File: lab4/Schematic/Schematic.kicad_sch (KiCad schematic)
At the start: 404 parts, among them IC1 TPS564252DRLR, IC2 TPS564252DRLR, IC3 TPS564252DRLR, IC4 TPS564252DRLR, IC5 TPS564252DRLR, IC6 TPS564252DRLR, J1 XT60-M, J10 CANA_Z1, J11 CANA_Z1, J12 CANA_Z1, J13 CANA_Z1, J14 CANA_Z1, J15 CANA_Z1, J16 Conn_01x03_Pin, J17 Conn_01x03_Pin, J2 Z2_SWD, J3 Z2_SWD, J4 Z3_USART, J5 Raspberry_Pi_4, J6 Z3_USART, J7 MOTOR_RIGHT, J8 MOTOR_LEFT, J9 SERVO, Q2 IRF4905, U1 MCP2515-xST, U10 SN65HVD230, U11 MCP2515-xST, U12 SN65HVD230, U13 MCP2515-xST, U14 SN65HVD230, U15 MCP2515-xST, U16 SN65HVD230, U17 MCP2515-xST, U18 SN65HVD230, U2 ACS712xLCTR-05B, U20 L298N, U3 STM32F401RETx, U4 ACS712xLCTR-05B, U5 INA181, U7 STM32F401RETx, U8 SN65HVD230, U9 MCP2515-xST, Y1 CX3225SB16000H0FLJCC, Y2 CX3225SB16000H0FLJCC, Y3 CX3225SB16000H0FLJCC, Y4 CX3225SB16000H0FLJCC, Y5 CX3225SB16000H0FLJCC, Y6 CX3225SB16000H0FLJCC, Y7 ABS25-32.768KHZ-6-T, Y8 ABS25-32.768KHZ-6-T

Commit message: Power input and protections done with pours.
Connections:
- net +12V: now also J16.3 (Pin_3), J17.3 (Pin_3); no longer J16.1 (Pin_1), J17.1 (Pin_1)
- net GND: now also J1.1 (NEG), J16.1 (Pin_1), J17.1 (Pin_1); no longer J1.N (NEG), J16.3 (Pin_3), J17.3 (Pin_3)
- net at F2.1_1, F2.1_2: now also J1.2 (POS); no longer J1.P (POS)
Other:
- moved on the sheet: J16, J17
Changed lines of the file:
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@@
 	(wire
 		(pts
+			(xy 53.34 91.44) (xy 60.96 91.44)
+		)
+		(stroke
+			(width 0)
+			(type default)
+		)
+	)
+	(wire
+		(pts
 			(xy 664.21 345.44) (xy 664.21 342.9)
 		)
@@
 	(wire
 		(pts
+			(xy 53.34 104.14) (xy 60.96 104.14)
+		)
+		(stroke
+			(width 0)
+			(type default)
+		)
+	)
+	(wire
+		(pts
 			(xy 505.46 448.31) (xy 505.46 450.85)
 		)
@@
 	(wire
 		(pts
+			(xy 43.18 86.36) (xy 60.96 86.36)
+		)
+		(stroke
+			(width 0)
+			(type default)
+		)
+	)
+	(wire
+		(pts
 			(xy 486.41 285.75) (xy 497.84 285.75)
 		)
@@
 	(wire
 		(pts
+			(xy 43.18 99.06) (xy 60.96 99.06)
+		)
+		(stroke
+			(width 0)
+			(type default)
+		)
+	)
+	(wire
+		(pts
 			(xy 123.19 396.24) (xy 123.19 417.83)
 		)
@@
 	(wire
 		(pts
-			(xy 60.96 99.06) (xy 43.18 99.06)
-		)
-		(stroke
-			(width 0)
-			(type default)
-		)
-	)
-	(wire
-		(pts
 			(xy 245.11 45.72) (xy 247.65 45.72)
 		)
@@
 	(wire
 		(pts
-			(xy 17.78 101.6) (xy 60.96 101.6)
-		)
-		(stroke
-			(width 0)
-			(type default)
-		)
-	)
-	(wire
-		(pts
 			(xy 458.47 280.67) (xy 466.09 280.67)
 		)
@@
 	(wire
 		(pts
-			(xy 53.34 91.44) (xy 60.96 91.44)
-		)
-		(stroke
-			(width 0)
-			(type default)
-		)
-	)
-	(wire
-		(pts
 			(xy 275.59 173.99) (xy 275.59 176.53)
 		)
@@
 	(wire
 		(pts
-			(xy 20.32 88.9) (xy 60.96 88.9)
-		)
-		(stroke
-			(width 0)
-			(type default)
-		)
-	)
-	(wire
-		(pts
 			(xy 365.76 207.01) (xy 365.76 219.71)
 		)
@@
 	(wire
 		(pts
-			(xy 60.96 86.36) (xy 43.18 86.36)
-		)
-		(stroke
-			(width 0)
-			(type default)
-		)
-	)
-	(wire
-		(pts
 			(xy 560.07 91.44) (xy 581.66 91.44)
 		)
@@
 	(wire
 		(pts
+			(xy 17.78 101.6) (xy 60.96 101.6)
+		)
+		(stroke
+			(width 0)
+			(type default)
+		)
+	)
+	(wire
+		(pts
 			(xy 436.88 419.1) (xy 485.14 419.1)
 		)
@@
 	(wire
 		(pts
-			(xy 53.34 104.14) (xy 60.96 104.14)
-		)
-		(stroke
-			(width 0)
-			(type default)
-		)
-	)
-	(wire
-		(pts
 			(xy 736.6 58.42) (xy 736.6 55.88)
 		)
@@
 	(wire
 		(pts
+			(xy 20.32 88.9) (xy 60.96 88.9)
+		)
+		(stroke
+			(width 0)
+			(type default)
+		)
+	)
+	(wire
+		(pts
 			(xy 60.96 444.5) (xy 97.79 444.5)
 		)
@@
 	(symbol
 		(lib_id "Connector:Conn_01x03_Pin")
-		(at 66.04 101.6 0)
-		(mirror y)
+		(at 66.04 101.6 180)
 		(unit 1)
 		(body_style 1)
@@
 		(dnp no)
 		(property "Reference" "J16"
-			(at 65.405 93.98 0)
+			(at 65.405 109.22 0)
 			(show_name no)
 			(do_not_autoplace no)
@@
 		)
 		(property "Value" "Conn_01x03_Pin"
-			(at 65.405 96.52 0)
+			(at 65.405 106.68 0)
 			(show_name no)
 			(do_not_autoplace no)
@@
 			)
 		)
-		(pin "N"
+		(pin "2"
 		)
-		(pin "P"
+		(pin "1"
 		)
 		(instances
@@
 	(symbol
 		(lib_id "Connector:Conn_01x03_Pin")
-		(at 66.04 88.9 0)
-		(mirror y)
+		(at 66.04 88.9 180)
 		(unit 1)
 		(body_style 1)
@@
 		(dnp no)
 		(property "Reference" "J17"
-			(at 65.405 81.28 0)
+			(at 65.405 96.52 0)
 			(show_name no)
 			(do_not_autoplace no)
@@
 		)
 		(property "Value" "Conn_01x03_Pin"
-			(at 65.405 83.82 0)
+			(at 65.405 93.98 0)
 			(show_name no)
 			(do_not_autoplace no)

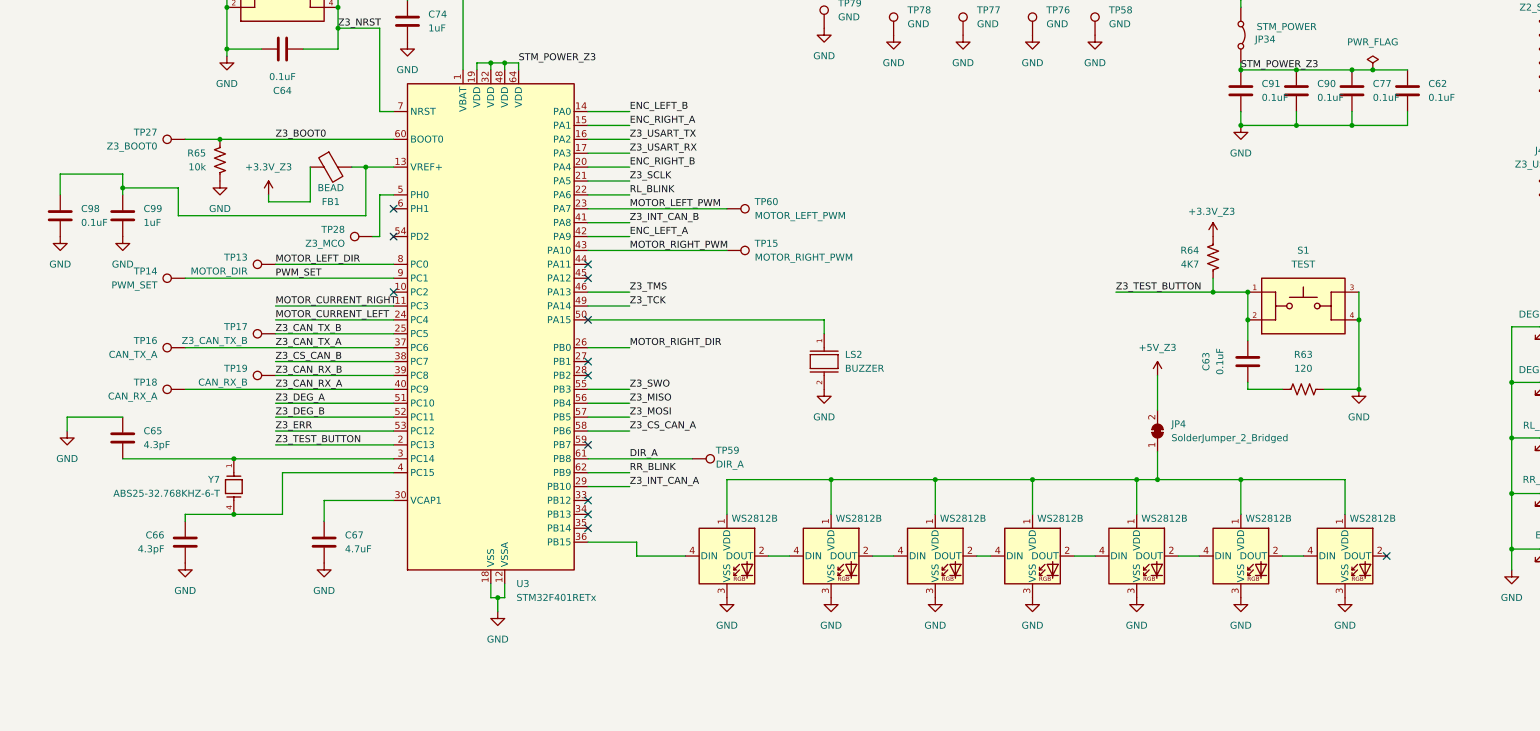
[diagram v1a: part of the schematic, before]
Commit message: Initial pin assignment change.
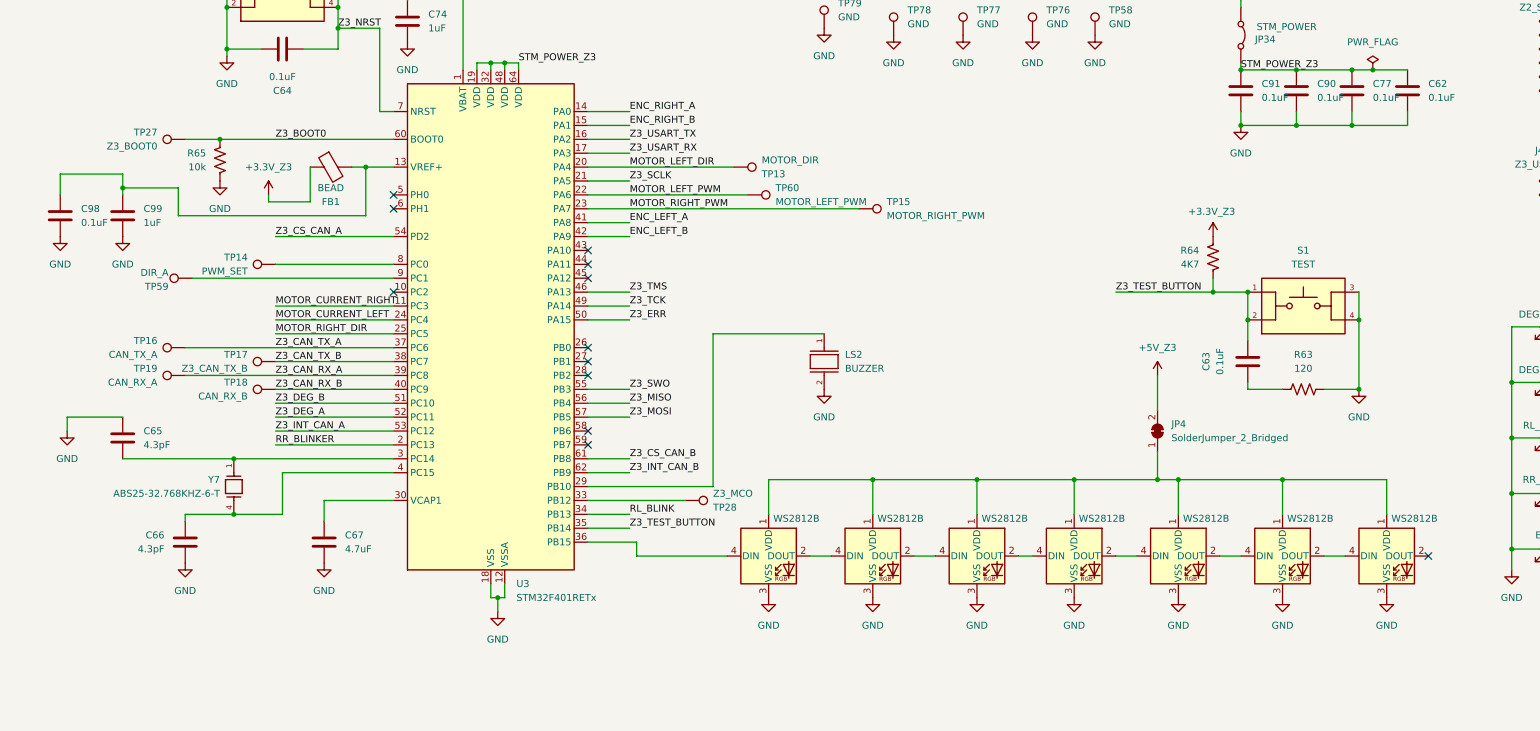
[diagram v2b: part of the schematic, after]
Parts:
- TP18: value CAN_RX_A -> CAN_RX_B
- TP19: value CAN_RX_B -> CAN_RX_A
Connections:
- net ENC_LEFT_A: now also U3.41 (PA8); no longer U3.42 (PA9)
- net ENC_LEFT_B: now also U3.42 (PA9); no longer U3.14 (PA0)
- net ENC_RIGHT_A: now also U3.14 (PA0); no longer U3.15 (PA1)
- net ENC_RIGHT_B: now also U3.15 (PA1); no longer U3.20 (PA4)
- net MOTOR_LEFT_DIR: now also U3.20 (PA4); no longer U3.8 (PC0)
- net MOTOR_LEFT_PWM: now also U3.22 (PA6); no longer U3.23 (PA7)
- net MOTOR_RIGHT_DIR: now also U3.25 (PC5); no longer U3.26 (PB0)
- net MOTOR_RIGHT_PWM: now also U3.23 (PA7); no longer U3.43 (PA10)
- net RL_BLINK: now also U3.34 (PB13); no longer U3.22 (PA6)
- net RR_BLINK: no longer U3.62 (PB9)
- net Z3_CAN_RX_A: now also TP19.1, U3.39 (PC8); no longer TP18.1, U3.40 (PC9)
- net Z3_CAN_RX_B: now also TP18.1, U3.40 (PC9); no longer TP19.1, U3.39 (PC8)
- net Z3_CAN_TX_B: now also U3.38 (PC7); no longer U3.25 (PC5)
- net Z3_CS_CAN_A: now also U3.54 (PD2); no longer U3.58 (PB6)
- net Z3_CS_CAN_B: now also U3.61 (PB8); no longer U3.38 (PC7)
- net Z3_DEG_A: now also U3.52 (PC11); no longer U3.51 (PC10)
- net Z3_DEG_B: now also U3.51 (PC10); no longer U3.52 (PC11)
- net Z3_ERR: now also U3.50 (PA15); no longer U3.53 (PC12)
- net Z3_INT_CAN_A: now also U3.53 (PC12); no longer U3.29 (PB10)
- net Z3_INT_CAN_B: now also U3.62 (PB9); no longer U3.41 (PA8)
- net Z3_TEST_BUTTON: now also U3.35 (PB14); no longer U3.2 (PC13)
- net at TP28.1: now also U3.33 (PB12); no longer U3.5 (PH0)
- net at LS2.1: now also U3.29 (PB10); no longer U3.50 (PA15)
- net DIR_A: no longer names the net of TP59.1
- net DIR_A: now also U3.9 (PC1); no longer U3.61 (PB8)
- net PWM_SET: no longer names the net of TP14.1
- net PWM_SET: now also U3.8 (PC0); no longer U3.9 (PC1)
- new net RR_BLINKER: U3.2 (PC13)
- no-connect marks 89 -> 88
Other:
- moved on the sheet: TP13, TP14, TP15, TP17, TP18, TP19, TP28, TP59, TP60

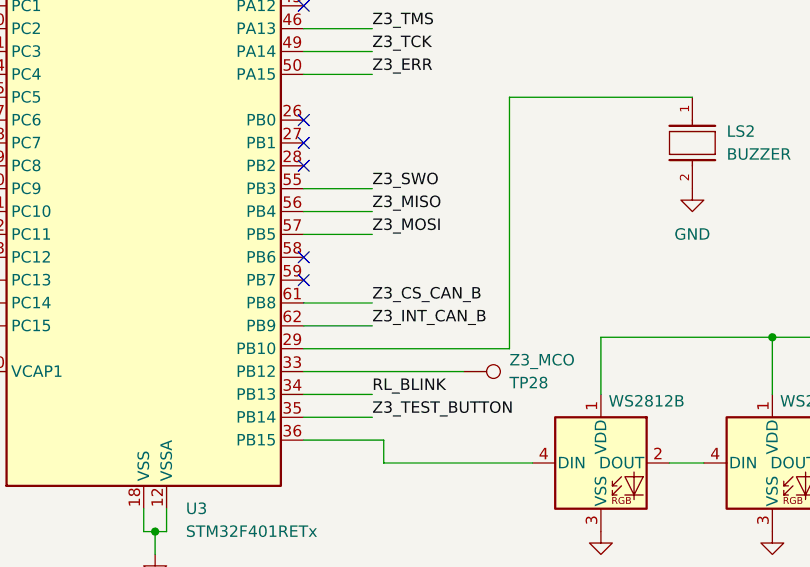
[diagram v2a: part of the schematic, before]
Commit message: Fixed ENC and CAN_INT exti cofnflict.
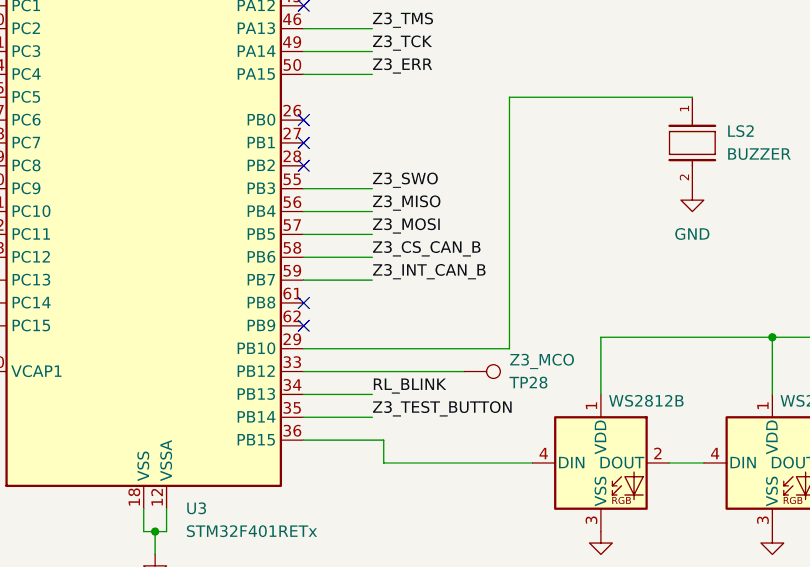
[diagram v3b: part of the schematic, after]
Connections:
- net Z3_CS_CAN_B: now also U3.58 (PB6); no longer U3.61 (PB8)
- net Z3_INT_CAN_B: now also U3.59 (PB7); no longer U3.62 (PB9)
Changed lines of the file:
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@@
 	)
 	(no_connect
-		(at 617.22 114.3)
-	)
-	(no_connect
 		(at 44.45 64.77)
 	)
@@
 	)
 	(no_connect
+		(at 617.22 119.38)
+	)
+	(no_connect
 		(at 267.97 222.25)
 	)
@@
 	)
 	(no_connect
-		(at 260.35 115.57)
+		(at 617.22 121.92)
 	)
 	(no_connect
-		(at 617.22 116.84)
+		(at 260.35 115.57)
 	)
 	(no_connect
@@
 	(wire
 		(pts
+			(xy 617.22 114.3) (xy 624.84 114.3)
+		)
+		(stroke
+			(width 0)
+			(type default)
+		)
+	)
+	(wire
+		(pts
 			(xy 713.74 88.9) (xy 731.52 88.9)
 		)
@@
 	(wire
 		(pts
-			(xy 624.84 121.92) (xy 617.22 121.92)
-		)
-		(stroke
-			(width 0)
-			(type default)
-		)
-	)
-	(wire
-		(pts
 			(xy 562.61 198.12) (xy 638.81 198.12)
 		)
@@
 	(wire
 		(pts
-			(xy 617.22 119.38) (xy 624.84 119.38)
-		)
-		(stroke
-			(width 0)
-			(type default)
-		)
-	)
-	(wire
-		(pts
 			(xy 110.49 64.77) (xy 114.3 64.77)
 		)
@@
 	(wire
 		(pts
+			(xy 617.22 116.84) (xy 624.84 116.84)
+		)
+		(stroke
+			(width 0)
+			(type default)
+		)
+	)
+	(wire
+		(pts
 			(xy 716.28 393.7) (xy 722.63 393.7)
 		)
@@
 	)
 	(label "Z3_CS_CAN_B"
-		(at 624.84 119.38 0)
+		(at 624.84 114.3 0)
 		(effects
 			(font
@@
 	)
 	(label "Z3_INT_CAN_B"
-		(at 624.84 121.92 0)
+		(at 624.84 116.84 0)
 		(effects
 			(font

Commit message: Logic level and v-reg for leds. Motor Driver heatsink. Fixed pth vs sm footprints. Misc.
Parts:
- added C101, C102: 4.7uF, Capacitor_SMD:C_0805_2012Metric, symbol Device:C
- added HS1: 6396BG, 449proj:HSINK_6396BG, symbol 449proj:6396BG
- added Q1, Q3: 2N7002, Package_TO_SOT_SMD:SOT-23, symbol Transistor_FET:2N7002
- added R100, R101, R102, R68, R99: 4K7, Resistor_SMD:R_0603_1608Metric, symbol Device:R_US
- added R37: 10k, Resistor_SMD:R_0603_1608Metric, symbol Device:R
- added R67: 47K, Resistor_SMD:R_0603_1608Metric, symbol Device:R
- added U6: AP7361EA-SPR-13, 449proj:AP7361EA_SO-8EP, symbol 449proj:AP7361EA-SPR-13
- C25, C26, C86: footprint Capacitor_THT:CP_Radial_D8.0mm_P3.80mm -> 449proj:CP_Elec_8x11.9_A768
- J7, J8: footprint Connector_JST:JST_PH_S6B-PH-K_1x06_P2.00mm_Horizontal -> Connector_JST:JST_PH_B6B-PH-SM4-TB_1x06-1MP_P2.00mm_Vertical
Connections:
- net RR_BLINKER is gone; now on net RR_BLINK: U3.2 (PC13)
- net +3.3V_Z2: now also Q1.1 (G), R99.1
- net +3.3V_Z3: now also Q3.1 (G), R101.1
- net +7V_Z2: now also C101.1, U6.5 (EN), U6.8 (IN); no longer JP3.2 (B)
- net GND: now also C101.2, C102.1, HS1.1, HS1.2, R37.2, U6.3 (GND), U6.9 (EP)
- net MOTOR_LEFT_DIR: now also U3.25 (PC5); no longer U3.20 (PA4)
- net MOTOR_LEFT_PWM: now also U3.23 (PA7); no longer U3.22 (PA6)
- net MOTOR_RIGHT_DIR: now also U3.20 (PA4); no longer U3.25 (PC5)
- net MOTOR_RIGHT_PWM: now also U3.22 (PA6); no longer U3.23 (PA7)
- net at D21.1 (VDD), D22.1 (VDD), D24.1 (VDD)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: now also R102.1
- net at D2.1 (VDD), D3.1 (VDD), D4.1 (VDD)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: now also R100.1
- net at D2.4 (DIN): now also Q1.3 (D), R100.2; no longer U7.36 (PB15)
- net at D8.4 (DIN): now also Q3.3 (D), R102.2; no longer U3.36 (PB15)
- new net: R67.1, R68.2
- new net: R37.1, R67.2, U6.2 (ADJ)
- new net: Q1.2 (S), R99.2, U7.36 (PB15)
- new net: C102.2, JP3.2 (B), R68.1, U6.1 (OUT)
- new net: U6.6 (NC), U6.7 (NC)
- new net: Q3.2 (S), R101.2, U3.36 (PB15)
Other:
- moved on the sheet: C73, JP3, R69, R70, S4, TP13, TP15, TP57, TP60

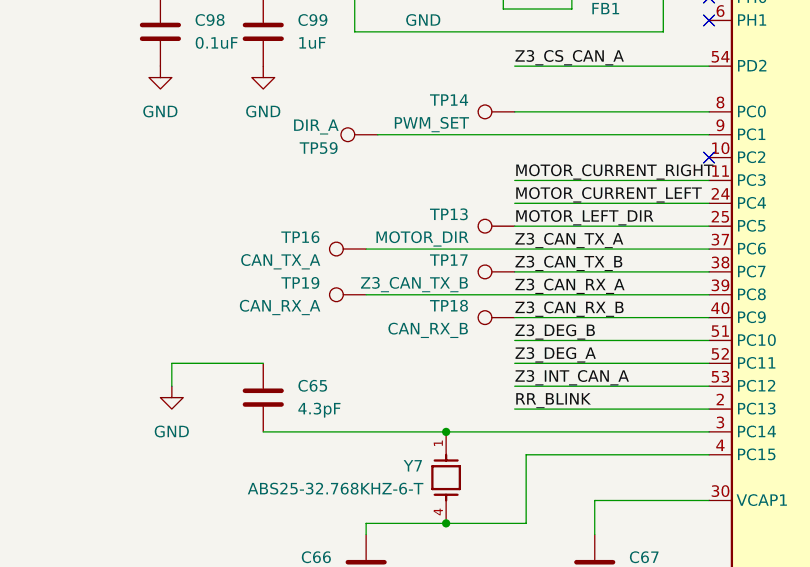
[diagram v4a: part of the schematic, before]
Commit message: Reworked ground at L298N
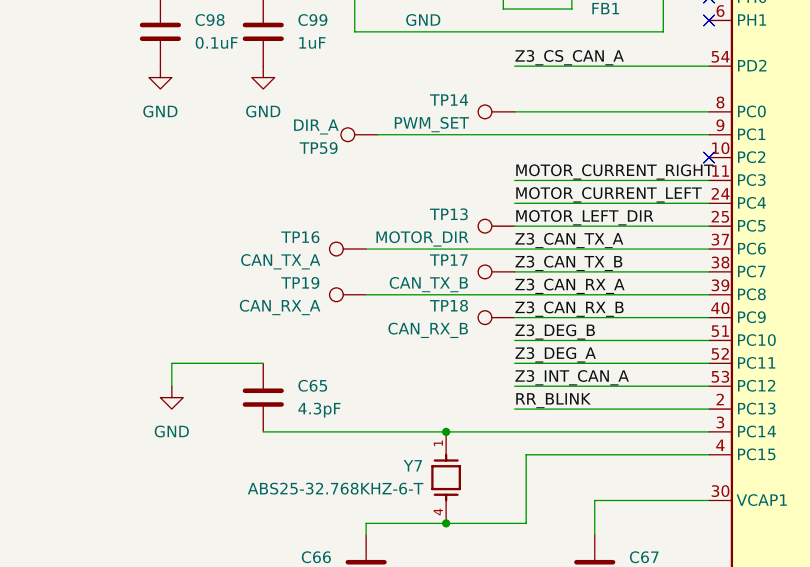
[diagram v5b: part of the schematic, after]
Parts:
- TP17: value Z3_CAN_TX_B -> CAN_TX_B
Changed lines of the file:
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@@
 			)
 		)
-		(property "Value" "Z3_CAN_TX_B"
+		(property "Value" "CAN_TX_B"
 			(at 554.99 102.8699 90)
 			(show_name no)
